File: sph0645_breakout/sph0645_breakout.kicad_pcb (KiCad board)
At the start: 2 copper layers, 15.5 x 7.5 mm, 3 parts, among them J1 GS3, J2 CONN_01X06, U1 SPH0645LM4H-B

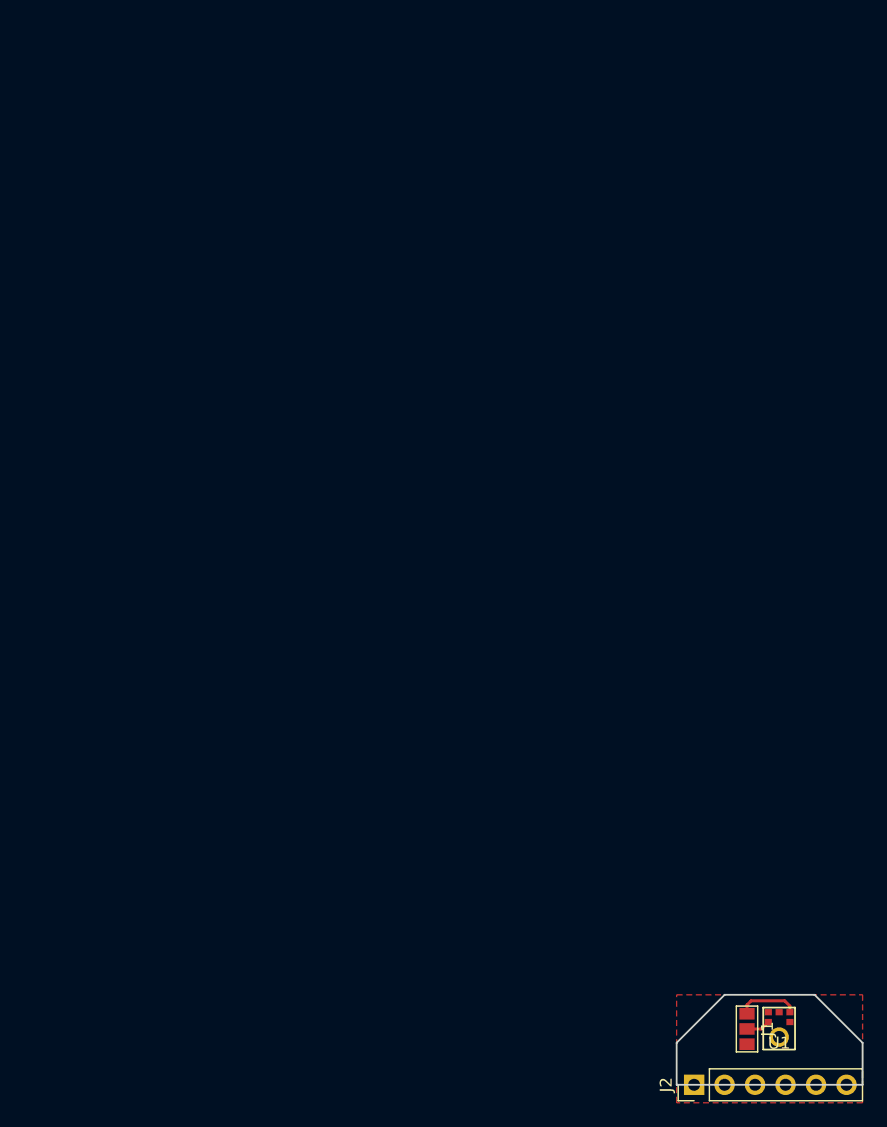
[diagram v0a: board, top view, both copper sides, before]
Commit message: Finished I2S microphone mod board
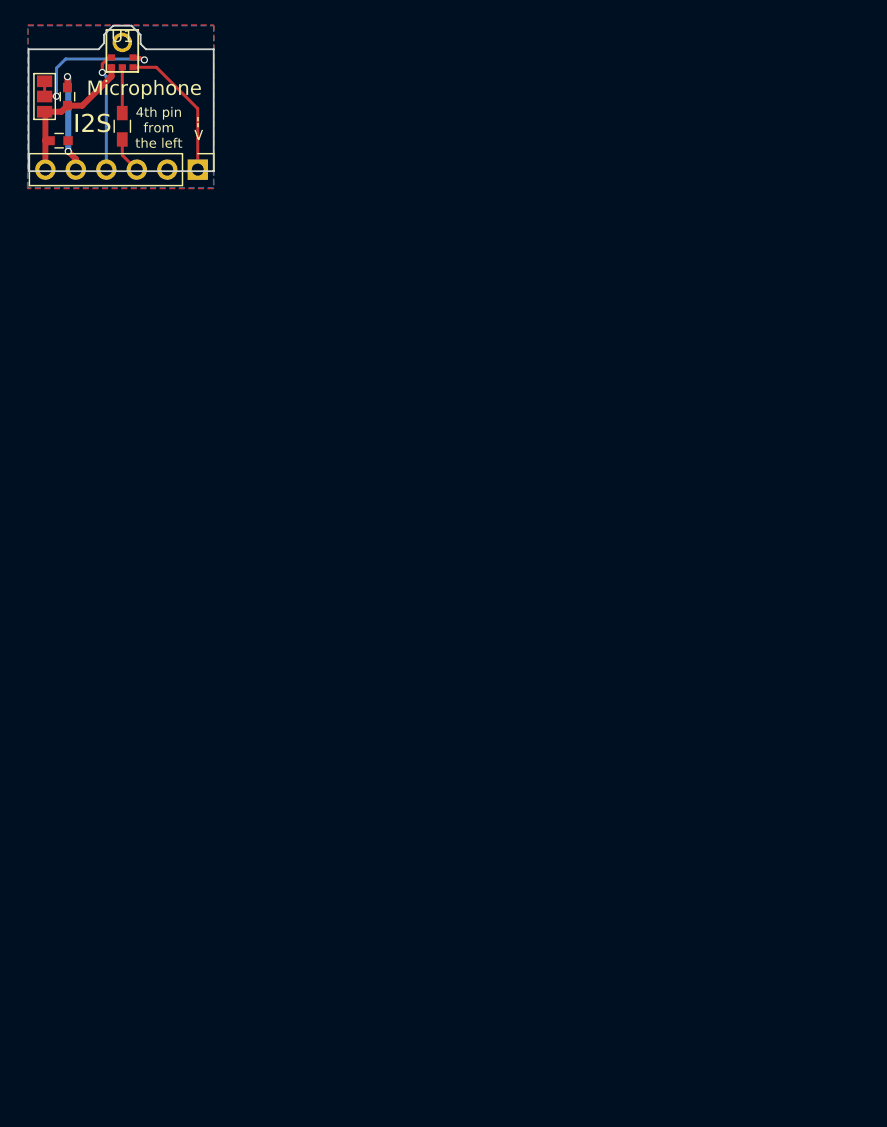
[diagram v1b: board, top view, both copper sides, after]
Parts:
- added C1: 100nF, Capacitors_SMD:C_0603, F.Cu at (77.0, 35.3)
- added C2: 30pF, Capacitors_SMD:C_0603, F.Cu at (77.7, 31.6)
- added R1: 47R, Resistors_SMD:R_0603_HandSoldering, F.Cu at (82.3, 34.1)
- moved U1 99.4 mm to (82.3, 27.1), turned to 180 degrees
- moved J1 97.3 mm to (75.8, 31.6), turned to 0 degrees
- moved J2 86.8 mm to (88.6, 37.7), turned to 270 degrees
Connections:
- J1 pad 2: Net-(J1-Pad2) -> GND
- J2 pad 1: (no net) -> WS
- J2 pad 3: (no net) -> DAT
- J2 pad 4: (no net) -> CLK
- J2 pad 5: (no net) -> GND
- J2 pad 6: (no net) -> +3V3
- U1 pad 1: (no net) -> WS
- U1 pad 2: Net-(J1-Pad2) -> GND
- U1 pad 4: (no net) -> CLK
- U1 pad 6: (no net) -> Net-(R1-Pad2)
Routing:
- net GND: track 0.00 -> 22.2 mm, vias 0 -> 4
- net WS: track 0.00 -> 11.9 mm
- net CLK: track 0.00 -> 9.94 mm, vias 0 -> 1
- net +3V3: track 5.15 -> 12.8 mm
- net Net-(R1-Pad2): track 0.00 -> 3.82 mm
- net DAT: track 0.00 -> 3.10 mm
- net Net-(J1-Pad2): track 2.02 -> 0.00 mm
- added copper zone on B.Cu, net GND
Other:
- board size 15.5 x 7.5 mm -> 15.4 x 12.1 mm
- board text added: "-->"
- board text added: "4th pin from the left"
- board text added: "I2S"
- board text added: "I2S microphone board Based on SPH0645 This side to back PCB"
- board text added: "Microphone"

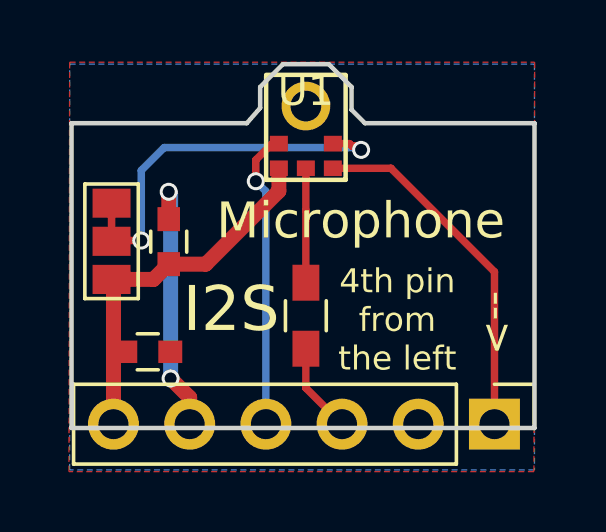
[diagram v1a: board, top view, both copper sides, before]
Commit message: No longer sticks out of the ZP outline, no longer flush to back PCB
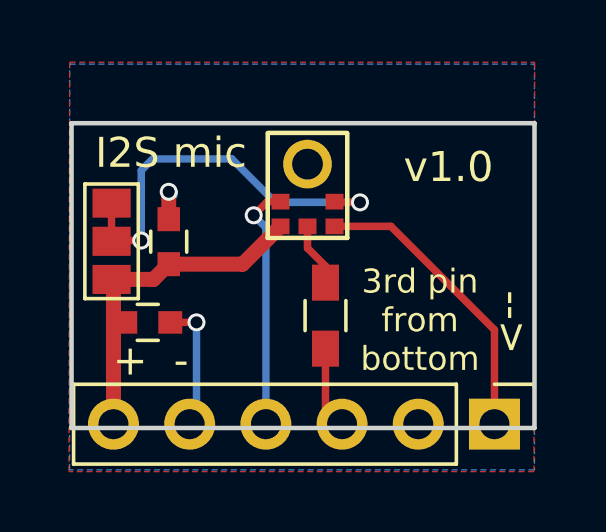
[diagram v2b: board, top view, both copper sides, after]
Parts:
- moved U1 1.94 mm to (82.3, 29.1)
- moved C1 0.98 mm to (77.0, 34.3)
- moved R1 0.65 mm to (83.0, 34.1)
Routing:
- net GND: track 22.2 -> 18.9 mm
- net WS: track 11.9 -> 9.91 mm
- net CLK: track 9.94 -> 8.21 mm
- net Net-(R1-Pad2): track 3.82 -> 2.12 mm
- net +3V3: track 12.8 -> 11.6 mm
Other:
- board size 15.4 x 12.1 mm -> 15.4 x 10.2 mm
- board text added: "+ -"
- board text added: "3rd pin from bottom"
- board text added: "I2S mic"
- board text added: "I2S microphone board Based on SPH0645 v1.0 This side to back PCB"
- board text added: "v1.0"
- board text removed: "4th pin from the left"
- board text removed: "I2S"
- board text removed: "I2S microphone board Based on SPH0645 This side to back PCB"
- board text removed: "Microphone"
